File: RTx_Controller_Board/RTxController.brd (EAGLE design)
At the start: 161.3 x 90.2 mm, 196 parts, among them IC2 MAX5984C, J22 Debug Header, SW1 COM08720, U1 STM32F407ZXT, U2 TPD4S012, U3 KSZ8081, X4 MINI-USB-32005-301, X8 0826-1X1T-GJ-F

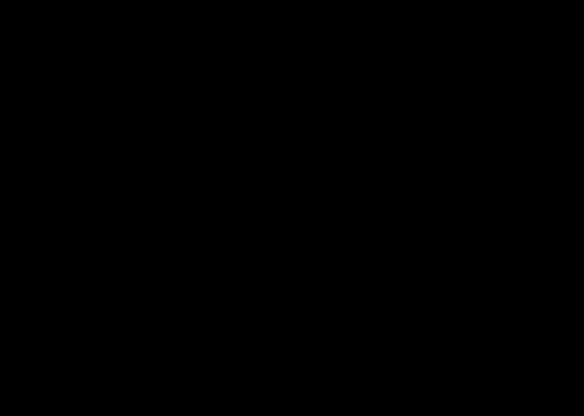
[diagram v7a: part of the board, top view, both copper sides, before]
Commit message: Updated controller schematic with high speed signal routing information. Added termination resistor to SPI_SCK line. Included Sightline documentation. Added avionics library, node4-2.lbr, to RTx controller library folder. Made progress on RTx_Charger board layout.
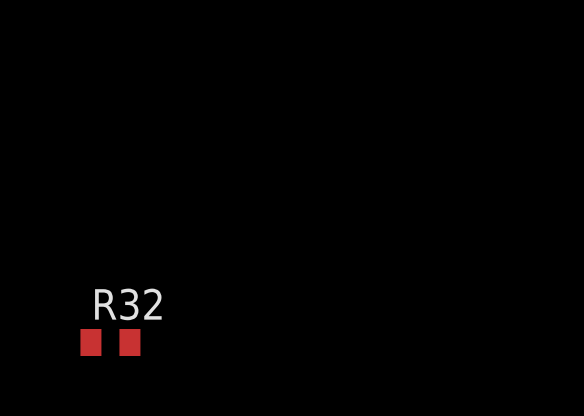
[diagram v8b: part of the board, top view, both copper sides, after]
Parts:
- added R32: 33, motorFeedback:R0402
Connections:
- new net N$72: R32.2, U1.30
- net SPI_SCK: now also R32.1; no longer U1.30
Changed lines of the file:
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@@
 <element name="C43" library="rcl" package="C0402" value="16p" x="3.81" y="80.01"/>
 <element name="C45" library="rcl" package="C0402" value="16p" x="12.7" y="80.01" rot="R270"/>
+<element name="R32" library="motorFeedback" package="R0402" value="33" x="-8.382" y="-12.192"/>
 </elements>
 <signals>
@@
 <contactref element="ADC1" pad="8"/>
 <contactref element="ADC4" pad="8"/>
-<contactref element="U1" pad="30"/>
 <wire x1="36.898" y1="19.05" x2="40.894" y2="19.05" width="0.3048" layer="1"/>
 <wire x1="40.894" y1="19.05" x2="41.148" y2="18.796" width="0.3048" layer="1"/>
@@
 <wire x1="39.116" y1="26.416" x2="40.894" y2="24.638" width="0.3048" layer="1"/>
 <wire x1="40.894" y1="24.638" x2="40.894" y2="19.05" width="0.3048" layer="1"/>
-<wire x1="41.148" y1="18.796" x2="60.77" y2="40.54" width="0" layer="19" extent="1-1"/>
-<wire x1="36.898" y1="42.418" x2="36.898" y2="35.052" width="0" layer="19" extent="1-1"/>
+<contactref element="R32" pad="1"/>
+<wire x1="36.898" y1="35.052" x2="36.898" y2="42.418" width="0" layer="19" extent="1-1"/>
+<wire x1="-9.032" y1="-12.192" x2="36.898" y2="19.05" width="0" layer="19" extent="1-1"/>
 </signal>
 <signal name="SPI_MISO">
@@
 <wire x1="57.05" y1="48.26" x2="12.7" y2="80.66" width="0" layer="19" extent="1-1"/>
 </signal>
+<signal name="N$72">
+<contactref element="R32" pad="2"/>
+<contactref element="U1" pad="30"/>
+<wire x1="-7.732" y1="-12.192" x2="60.77" y2="40.54" width="0" layer="19" extent="1-1"/>
+</signal>
 </signals>
